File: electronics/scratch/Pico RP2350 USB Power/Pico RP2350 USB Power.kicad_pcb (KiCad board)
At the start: 4 copper layers, 75 x 63 mm, 47 parts, among them J1 RFM69HCW, J10 IR TX AOE, J11 IR RX 1, J12 IR RX 2, J13 IR RX 3, J14 BUTTON A, J15 BUTTON B, J16 LED STRIP 1, J17 LED STRIP 2, J18 LED STRIP 3, J19 LED STRIP 4, J2 SD CARD, J20 LED STRIP 5, J21 LED STRIP 6, J22 POWER, J3 I2C_1, J4 I2C_2, J5 I2C_3, J6 STEMMA, J7 I2S AMP, J8 IR TX LINE, J9 IR TX CONE, Q1 AO3406, Q2 AO3406, Q3 AO3406, Q4 AO3401A, Q5 C20917, U1 74HCT244

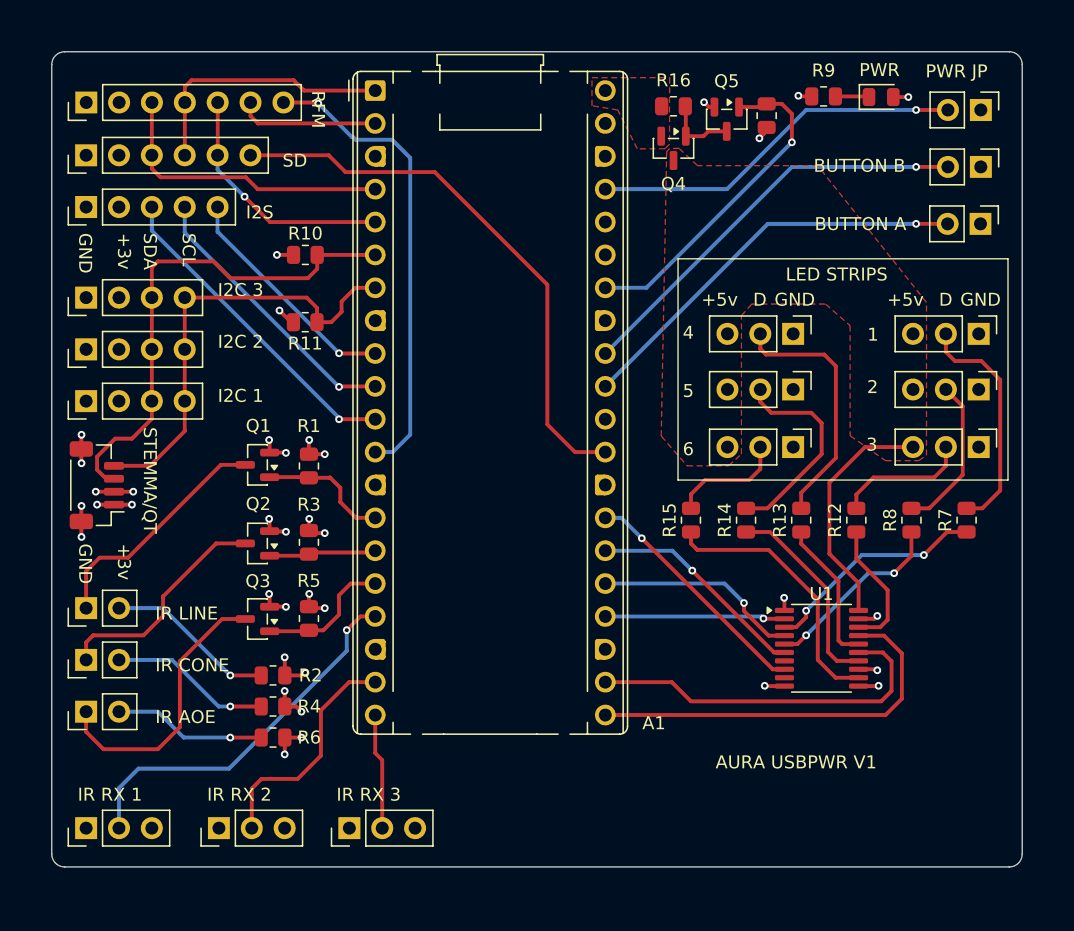
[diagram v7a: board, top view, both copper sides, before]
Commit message: RP2350 final adjustments before JLCPCB run
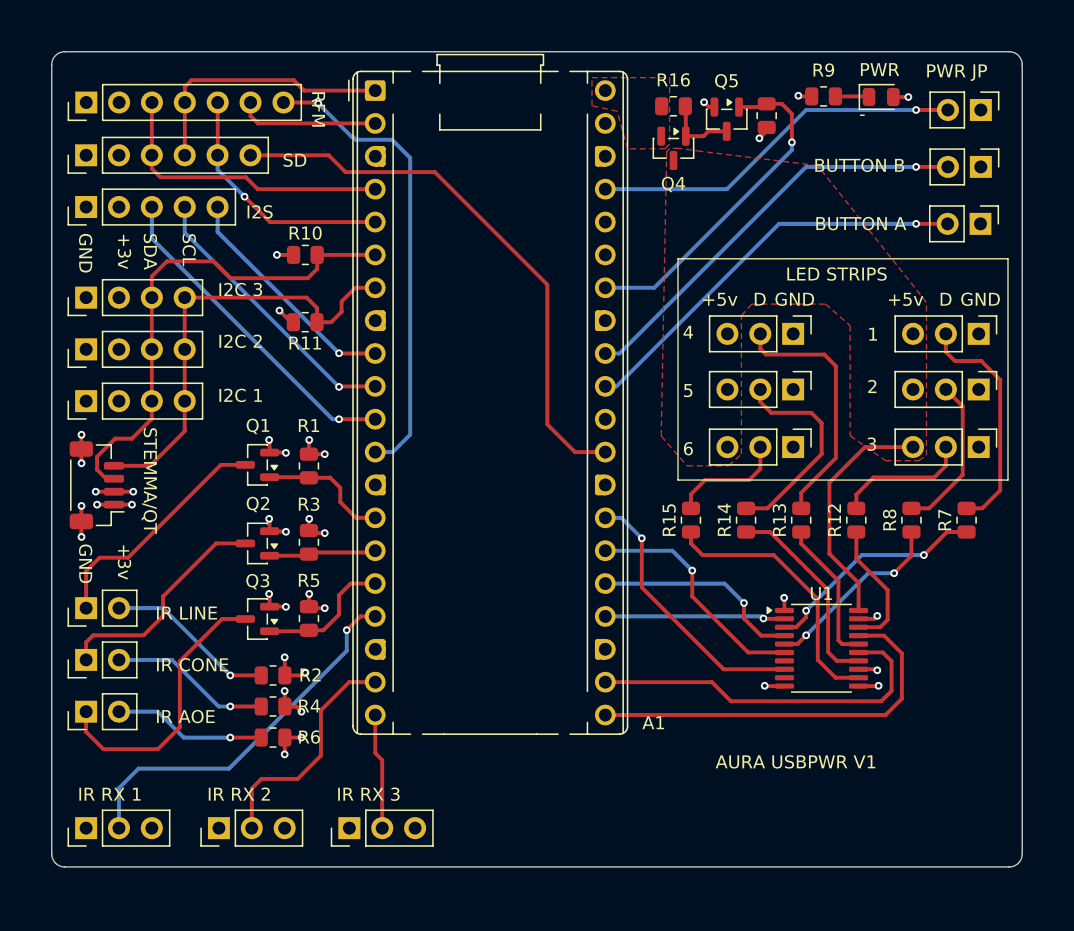
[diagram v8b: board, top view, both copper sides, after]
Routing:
- net /LED STRIP 6: track 18.7 -> 20.9 mm
- net /LED STRIP 5: track 17.1 -> 18.3 mm
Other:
- board text added: "-"
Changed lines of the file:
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@@
 		)
 	)
+	(gr_text "-"
+		(at 177.4 46.4 0)
+		(layer "F.SilkS")
+		(effects
+			(font
+				(size 1 1)
+				(thickness 0.15)
+			)
+			(justify left bottom)
+		)
+	)
 	(gr_text "3"
 		(at 177.94 71.95 0)
@@
 	)
 	(segment
-		(start 127.5 57.2)
-		(end 123.2 57.2)
-		(width 0.3)
-		(layer "F.Cu")
-		(net "/SDA")
-	)
-	(segment
 		(start 118.5 72.3)
 		(end 118.5 73.3)
@@
 	)
 	(segment
-		(start 128.8 58.5)
-		(end 127.5 57.2)
+		(start 122.735 58.365)
+		(end 122.735 60)
 		(width 0.3)
 		(layer "F.Cu")
@@
 	)
 	(segment
-		(start 123.2 57.2)
-		(end 122.735 57.665)
+		(start 128.8 58.5)
+		(end 127.5 57.2)
 		(width 0.3)
 		(layer "F.Cu")
@@
 	)
 	(segment
-		(start 134.8 58.5)
-		(end 128.8 58.5)
+		(start 127.5 57.2)
+		(end 123.9 57.2)
 		(width 0.3)
 		(layer "F.Cu")
@@
 	)
 	(segment
-		(start 122.735 57.665)
-		(end 122.735 60)
+		(start 123.9 57.2)
+		(end 122.735 58.365)
+		(width 0.3)
+		(layer "F.Cu")
+		(net "/SDA")
+	)
+	(segment
+		(start 134.8 58.5)
+		(end 128.8 58.5)
 		(width 0.3)
 		(layer "F.Cu")
@@
 	)
 	(segment
-		(start 137.2 69.3)
-		(end 122.735 54.835)
+		(start 137.2 69.4)
+		(end 136.7 69.4)
 		(width 0.3)
 		(layer "B.Cu")
@@
 	)
 	(segment
-		(start 137.2 69.4)
-		(end 137.2 69.3)
+		(start 136.7 69.4)
+		(end 122.735 55.435)
 		(width 0.3)
 		(layer "B.Cu")
@@
 	)
 	(segment
-		(start 122.735 54.835)
+		(start 122.735 55.435)
 		(end 122.735 53)
 		(width 0.3)
@@
 	)
 	(segment
+		(start 161.56 59.24)
+		(end 157.78 59.24)
+		(width 0.3)
+		(layer "B.Cu")
+		(net "/5V_ENABLE")
+	)
+	(segment
 		(start 172.2 48)
-		(end 160.96 59.24)
+		(end 172.2 48.6)
 		(width 0.3)
 		(layer "B.Cu")
@@
 	)
 	(segment
-		(start 160.96 59.24)
-		(end 157.78 59.24)
+		(start 172.2 48.6)
+		(end 161.56 59.24)
 		(width 0.3)
 		(layer "B.Cu")
@@
 	)
 	(segment
-		(start 170.405761 86.125)
-		(end 168.5 84.219239)
+		(start 171.625 86.125)
+		(end 169.825 86.125)
 		(width 0.3)
 		(layer "F.Cu")
@@
 	)
 	(segment
-		(start 171.625 86.125)
-		(end 170.405761 86.125)
+		(start 169.825 86.125)
+		(end 168.5 84.8)
 		(width 0.3)
 		(layer "F.Cu")
@@
 	)
 	(segment
-		(start 168.5 84.219239)
+		(start 168.5 84.8)
 		(end 168.5 83.6)
 		(width 0.3)
@@
 	)
 	(segment
-		(start 170.825 87.425)
+		(start 168.825 87.425)
+		(end 164.5 83.1)
+		(width 0.3)
+		(layer "F.Cu")
+		(net "/LED STRIP 5")
+	)
+	(segment
+		(start 164.5 83.1)
 		(end 164.5 81.1)
 		(width 0.3)
@@
 	(segment
 		(start 171.625 87.425)
-		(end 170.825 87.425)
+		(end 168.825 87.425)
 		(width 0.3)
 		(layer "F.Cu")
@@
 	)
 	(segment
-		(start 170.725 88.725)
+		(start 160.6 82.4)
 		(end 160.6 78.6)
 		(width 0.3)
@@
 	)
 	(segment
+		(start 166.925 88.725)
+		(end 160.6 82.4)
+		(width 0.3)
+		(layer "F.Cu")
+		(net "/LED STRIP 6")
+	)
+	(segment
 		(start 171.625 88.725)
-		(end 170.725 88.725)
+		(end 166.925 88.725)
 		(width 0.3)
 		(layer "F.Cu")
@@
 	)
 	(segment
-		(start 164.4 78.1125)
-		(end 164.4 79)
+		(start 164.4 79)
+		(end 165.3 79.9)
 		(width 0.3)
 		(layer "F.Cu")
@@
 	)
 	(segment
-		(start 174.2 88)
-		(end 175.575 89.375)
+		(start 164.4 78.1125)
+		(end 164.4 79)
 		(width 0.3)
 		(layer "F.Cu")
@@
 	)
 	(segment
-		(start 170.4 79.5)
-		(end 174.2 83.3)
+		(start 165.3 79.9)
+		(end 170.8 79.9)
 		(width 0.3)
 		(layer "F.Cu")
@@
 	)
 	(segment
-		(start 164.9 79.5)
-		(end 170.4 79.5)
+		(start 174.2 88)
+		(end 175.575 89.375)
 		(width 0.3)
 		(layer "F.Cu")
@@
 	)
 	(segment
-		(start 164.4 79)
-		(end 164.9 79.5)
+		(start 170.8 79.9)
+		(end 174.2 83.3)
 		(width 0.3)
 		(layer "F.Cu")
@@
 	)
 	(segment
-		(start 162.92 89.72)
-		(end 157.78 89.72)
+		(start 167.5 91.2)
+		(end 166.02 89.72)
 		(width 0.3)
 		(layer "F.Cu")
@@
 	)
 	(segment
-		(start 179.9 88.1)
-		(end 179.9 90.4)
+		(start 179.225 87.425)
+		(end 179.9 88.1)
 		(width 0.3)
 		(layer "F.Cu")
@@
 	)
 	(segment
-		(start 179.1 91.2)
-		(end 164.4 91.2)
+		(start 177.35 87.425)
+		(end 179.225 87.425)
 		(width 0.3)
 		(layer "F.Cu")
@@
 	)
 	(segment
-		(start 179.225 87.425)
-		(end 179.9 88.1)
+		(start 179.9 88.1)
+		(end 179.9 90.4)
 		(width 0.3)
 		(layer "F.Cu")
@@
 	)
 	(segment
-		(start 164.4 91.2)
-		(end 162.92 89.72)
+		(start 179.1 91.2)
+		(end 167.5 91.2)
 		(width 0.3)
 		(layer "F.Cu")
@@
 	)
 	(segment
-		(start 177.35 87.425)
-		(end 179.225 87.425)
+		(start 166.02 89.72)
+		(end 157.78 89.72)
 		(width 0.3)
 		(layer "F.Cu")
@@
 	)
 	(segment
-		(start 181.8 49.9)
-		(end 172.2 49.9)
+		(start 173.3 49.9)
+		(end 158.88 64.32)
 		(width 0.3)
 		(layer "B.Cu")
@@
 	)
 	(segment
-		(start 172.2 49.9)
+		(start 158.88 64.32)
 		(end 157.78 64.32)
 		(width 0.3)
@@
 	)
 	(segment
+		(start 181.8 49.9)
+		(end 173.3 49.9)
+		(width 0.3)
+		(layer "B.Cu")
+		(net "/BUTTON B")
+	)
+	(segment
 		(start 140 84.64)
 		(end 138.86 84.64)
@@
 	)
 	(segment
-		(start 170.34 54.3)
+		(start 171.2 54.3)
+		(end 158.64 66.86)
+		(width 0.3)
+		(layer "B.Cu")
+		(net "/BUTTON A")
+	)
+	(segment
+		(start 158.64 66.86)
 		(end 157.78 66.86)
 		(width 0.3)
@@
 	(segment
 		(start 181.8 54.3)
-		(end 170.34 54.3)
+		(end 171.2 54.3)
 		(width 0.3)
 		(layer "B.Cu")
@@
 		(polygon
 			(pts
-				(xy 182 72.6) (xy 182.6 72.2) (xy 182.6 60.369696) (xy 174.195181 49.8) (xy 164.908146 49.8) (xy 163.470556 48.460169)
+				(xy 182 72.6) (xy 182.6 72.2) (xy 182.6 60.369696) (xy 174.195181 49.8) (xy 165.2 48.7) (xy 163.470556 48.460169)
 				(xy 162.744712 48.484148) (xy 162.522567 48.727118) (xy 162.1 70.7) (xy 164.1 73) (xy 167.3 73)
 				(xy 168.3 72.1) (xy 168.3 61.4) (xy 169.1 60.5) (xy 174.8 60.5) (xy 176.696926 62.15981) (xy 176.703097 70.672774)
@@
 		(polygon
 			(pts
-				(xy 156.75 43) (xy 162.75 43) (xy 162.745712 48.145712) (xy 162.395712 48.495712) (xy 160.25 48.5)
-				(xy 158.75 45.5) (xy 156.750001 45.166668) (xy 156.749999 45.166667)
+				(xy 156.75 43) (xy 162.75 43) (xy 162.745712 48.145712) (xy 162.395712 48.495712) (xy 159.5 48.5)
+				(xy 158.7 45.6) (xy 156.750001 45.166668) (xy 156.749999 45.166667)
 			)
 		)
